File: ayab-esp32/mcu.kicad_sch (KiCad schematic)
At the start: 29 parts, among them J201 SPARE1, J202 SPARE0, Q201 AO3400A, SW201 USER, SW202 RESET, SW203 BOOTSEL, U201 ESP32-S3-MINI-1

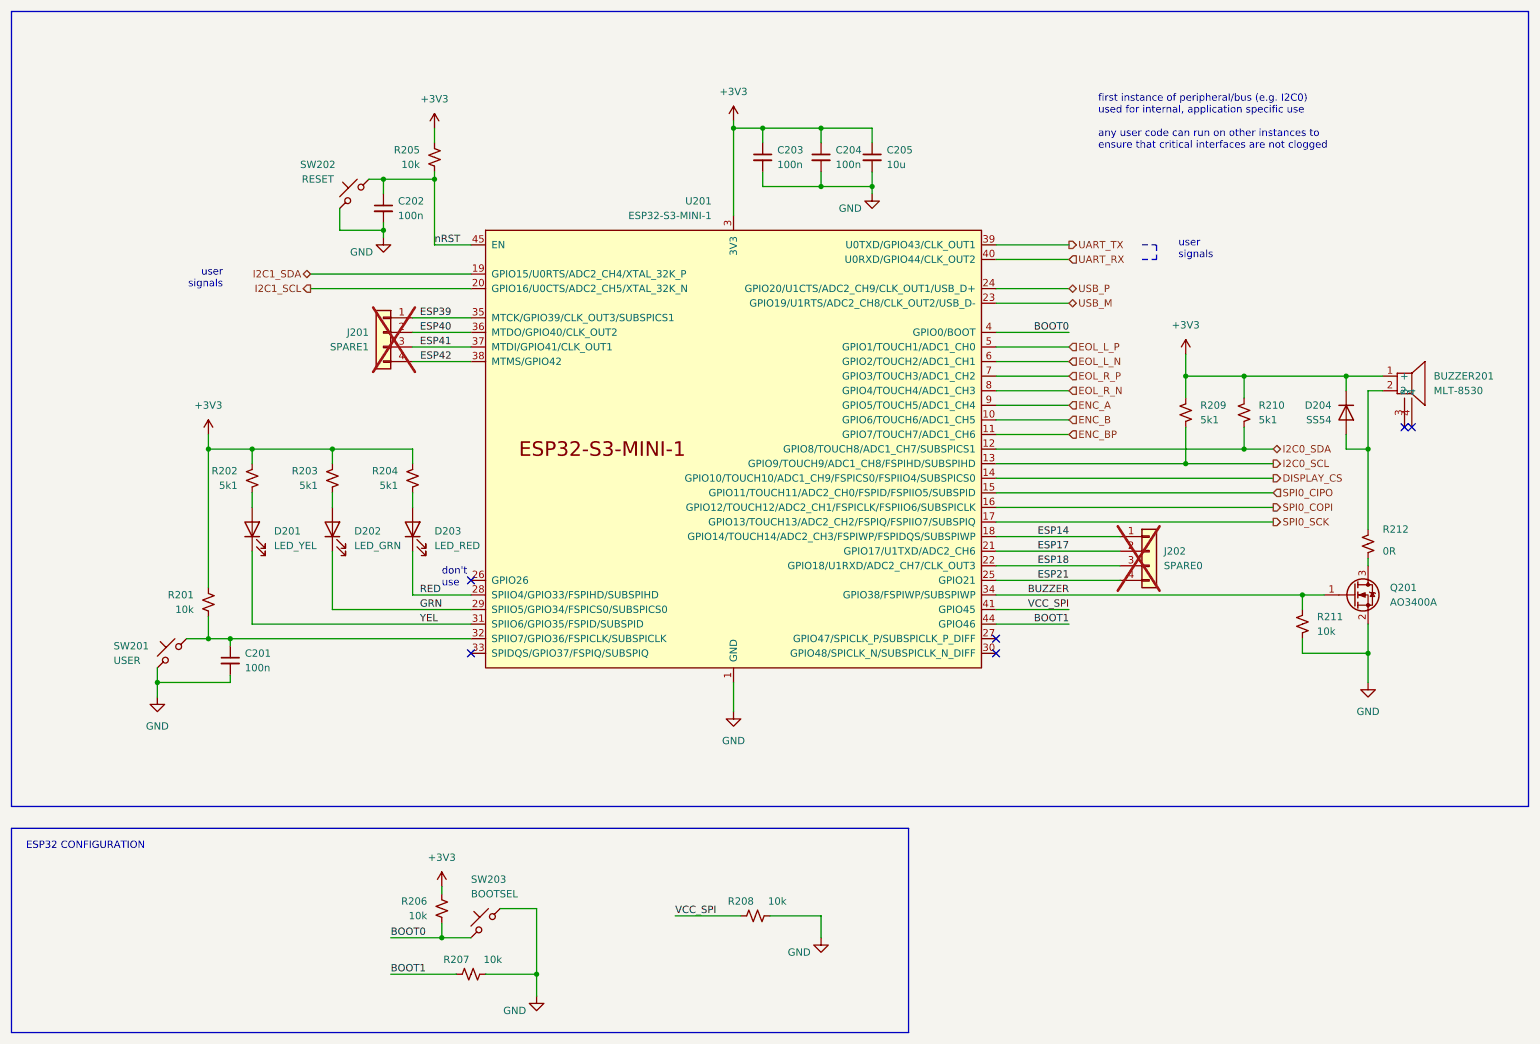
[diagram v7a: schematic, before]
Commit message: revise connector positions
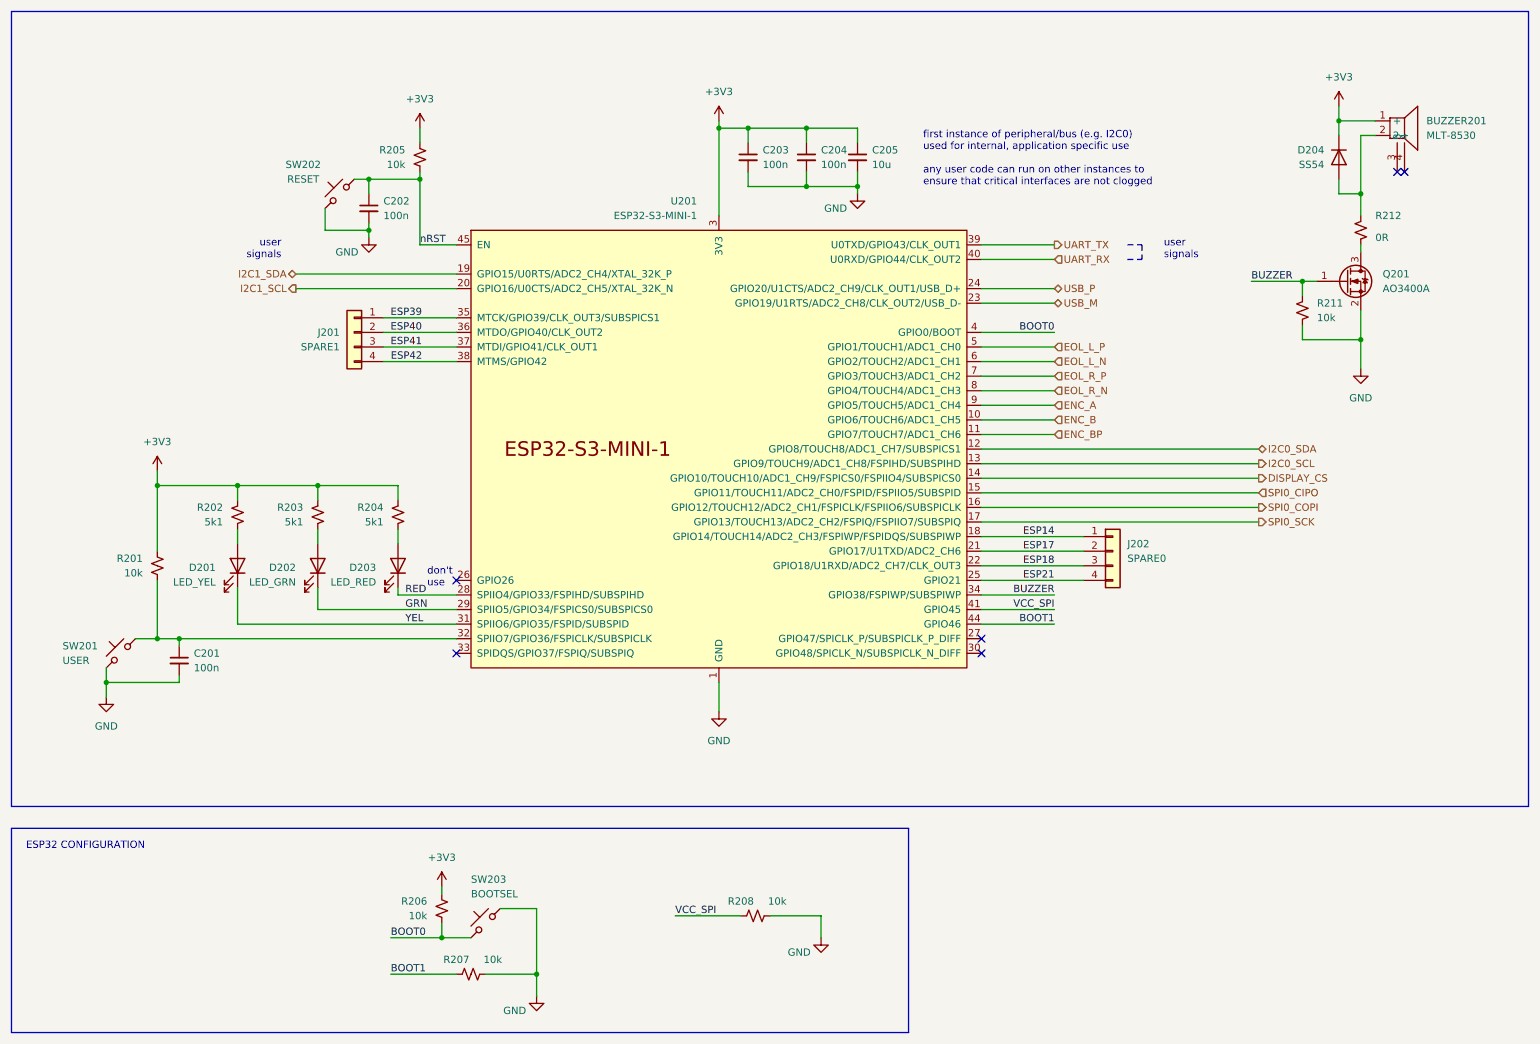
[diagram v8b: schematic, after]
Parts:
- removed R209, R210: 5k1, Resistor_SMD:R_0603_1608Metric, symbol ayab-lib:R_Small_US
- J201, J202: LCSC ID (none) -> C7501292; OEM (none) -> Megastar; OEM PN (none) -> ZX-PZ2.54-1-4PWZ; now fitted; now in the parts list
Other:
- moved on the sheet: BUZZER201, C201, C202, C203, C204, C205, D201, D202, D203, D204, Q201, R201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
